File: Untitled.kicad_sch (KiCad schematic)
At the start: 55 parts, among them J2 Conn_02x03_Odd_Even, J3 Conn_02x08_Odd_Even, J4 CONN_01X14, J5 CONN_01X14, Q1 LM317AG-TN3-R, SW1 SW_Push, U1 ICE40LP8K-CM121, U10 W25Q128JVSIQTR, U11 TYPE-C_24P_QCHT, U12 DSC1001DI5-024_0000, U2 TYPE-C_24P_QCHT, U3 TS-1187A-B-A-B, U4 iCE40-LP8K-CM81, U5 DSC6001CI2A-016.0000T, U6 AT25SF081-SSHD-B, U7 XC6206P332MR, U8 TYPE-C_24P_QCHT, U9 TYPE-C_24P_QCHT

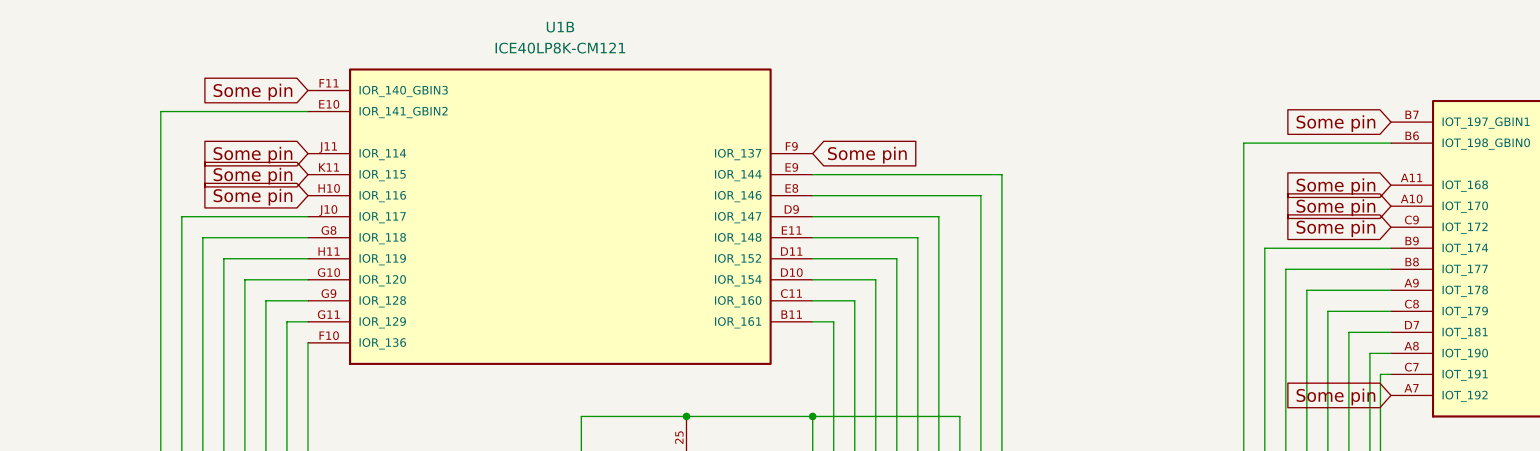
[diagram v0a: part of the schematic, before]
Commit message: Hook up USB 2 d and USB 3 tx+rx
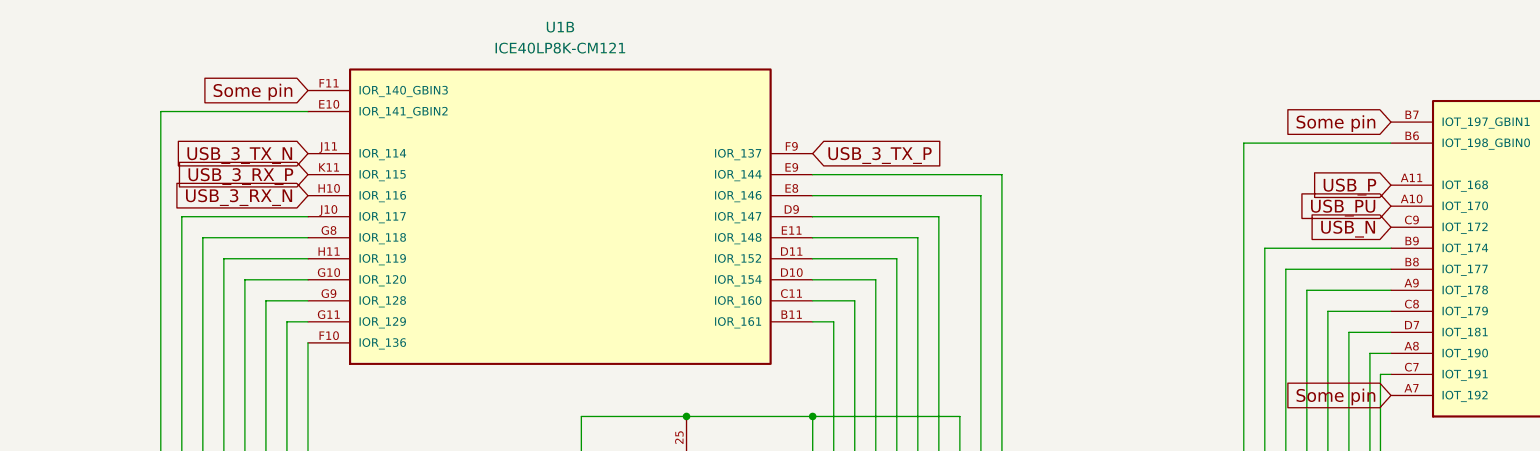
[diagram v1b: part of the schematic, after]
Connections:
- net Some pin: no longer U1.A10 (IOT_170), U1.A11 (IOT_168), U1.C9 (IOT_172), U1.F9 (IOR_137), U1.H10 (IOR_116), U1.J11 (IOR_114), U1.K11 (IOR_115)
- net USB_3_RX_N: now also U1.H10 (IOR_116)
- net USB_3_RX_P: now also U1.K11 (IOR_115)
- net USB_3_TX_N: now also U1.J11 (IOR_114)
- net USB_3_TX_P: now also U1.F9 (IOR_137)
- net USB_N: now also U1.C9 (IOT_172)
- net USB_P: now also U1.A11 (IOT_168)
- net USB_PU: now also U1.A10 (IOT_170)

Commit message: Swap bank 2 breakout for 2x USB2.0 connectors + IO
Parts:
- added C18: 10uF, Capacitors_SMD:C_0603, symbol TinyFPGA-BX-rescue:C
- added L2: Bead, Inductors_SMD:L_0603, symbol TinyFPGA-BX-rescue:Ferrite_Bead_Small
- added R15, R20, R25: 1.5k, Resistors_SMD:R_0402_NoSilk, symbol TinyFPGA-BX-rescue:R
- added R16, R17, R18, R19, R23, R24: 68, Resistors_SMD:R_0402_NoSilk, symbol TinyFPGA-BX-rescue:R
- added R21, R22, R26, R27: 5.1k, Resistors_SMD:R_0402_NoSilk, symbol TinyFPGA-BX-rescue:R
- added U13: TYPE-C_24P_QCHT, footprint:TYPE-C-SMD_TYPE-C-24P-QCHT, symbol TYPE-C_24P_QCHT:TYPE-C_24P_QCHT
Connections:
- net +5V: now also L2.1
- net GND: now also R2.1, R3.2, U8.A6 (D+), U8.B6 (D+), C18.1, R21.1, R22.1, R26.1, R27.1, U13.25 (EH), U13.A1 (GND), U13.A12 (GND), U13.B1 (GND), U13.B12 (GND)
- net LED: now also U1.J3 (IOB_57), U1.K4 (IOB_73), U1.L1 (IOB_56), U1.L2 (IOB_61), U1.L4 (IOB_72)
- net Some pin: now also U1.H9 (IOB_104_CBSEL1); no longer U1.L3 (IOB_71)
- net USB_N: now also R17.1
- net USB_P: now also R16.1
- net USB_PU: now also R15.2
- net at U2.B10 (RX1-): no longer U1.H7 (IOB_87)
- net at U2.A2 (TX1+): no longer U1.H9 (IOB_104_CBSEL1)
- net at U2.A7 (D-): now also U2.B7 (D-), R23.1; no longer U1.J3 (IOB_57)
- net at U2.A3 (TX1-): no longer U1.J4 (IOB_64)
- net at U2.B6 (D+): now also U2.A6 (D+), R24.2, R25.1; no longer U1.J5 (IOB_78)
- net at U2.B8 (SBU2): no longer U1.J7 (IOB_86)
- net at U2.A11 (RX2+): no longer U1.J8 (IOB_91)
- net at U2.A5 (CC1): now also R26.2; no longer U1.K3 (IOB_63)
- net at U2.B5 (CC2): now also R27.2; no longer U1.K4 (IOB_73)
- net Button: now reaches U1.K5 (IOB_79)
- net Button: now also U1.H7 (IOB_87), U1.J5 (IOB_78), U1.J7 (IOB_86), U1.K6 (IOB_82_GBIN4); no longer U2.B7 (D-)
- net at U2.B2 (TX2+): no longer U1.K6 (IOB_82_GBIN4)
- net at U2.B11 (RX1+): no longer U1.K7 (IOB_89)
- net at U2.A8 (SBU1): no longer U1.L1 (IOB_56)
- net at U2.B3 (TX2-): no longer U1.L4 (IOB_72)
- net at U2.A10 (RX2-): no longer U1.L7 (IOB_94)
- net at U2.A4 (VBUS): now also U2.A9 (VBUS), U2.B4 (VBUS), U2.B9 (VBUS), C18.2, L2.2, U13.A4 (VBUS), U13.A9 (VBUS), U13.B4 (VBUS), U13.B9 (VBUS)
- new net: R21.2, U13.A5 (CC1)
- new net: R19.2, R20.1, U13.A6 (D+), U13.B6 (D+)
- new net: R18.1, U13.A7 (D-), U13.B7 (D-)
- new net: R22.2, U13.B5 (CC2)
- new net: R15.1, R16.2
- new net USB_N_2: R18.2, U1.K3 (IOB_63)
- new net USB_N_3: R23.2, U1.K7 (IOB_89)
- new net USB_PU_2: R20.2, U1.L3 (IOB_71)
- new net USB_PU_3: R25.2, U1.J8 (IOB_91)
- new net USB_P_2: R19.1, U1.J4 (IOB_64)
- new net USB_P_3: R24.1, U1.L7 (IOB_94)
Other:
- note added: "2 button array?"
- moved on the sheet: U10, U12
